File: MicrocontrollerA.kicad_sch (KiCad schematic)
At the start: 35 parts, among them J1 SWD Connector, J13 USB_B_Micro, SW1 SW_Push, SW2 SW_SPDT, SW3 SW_SPDT, U1 STM32F446RCTx, U5 TVS0500DRV, Y1 25 MHz

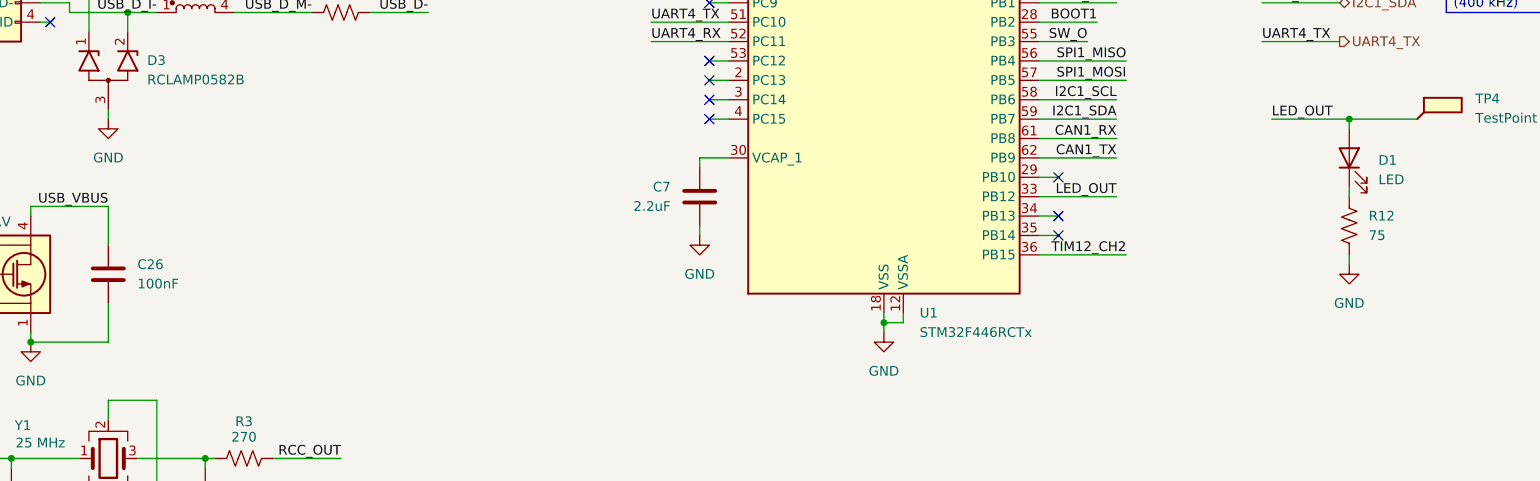
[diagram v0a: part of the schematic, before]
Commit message: Switch from variable to fixed 3.3V buck converter
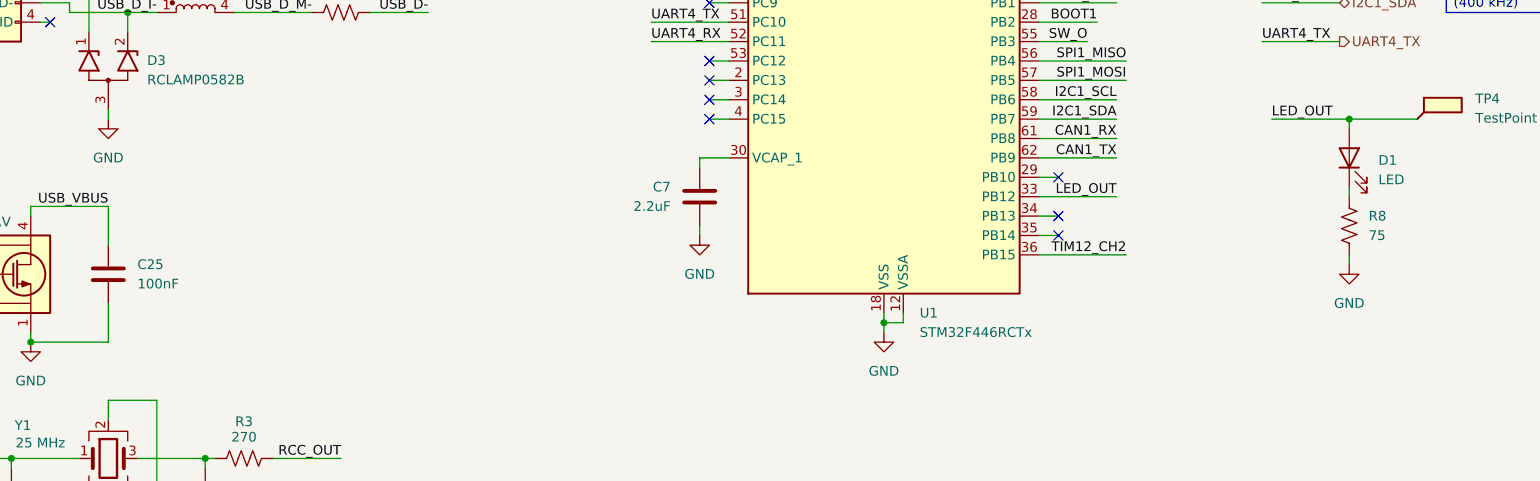
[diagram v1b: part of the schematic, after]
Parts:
- renumbered C26 to C25, R12 to R8
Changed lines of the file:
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@@
 		(dnp no)
 		(fields_autoplaced yes)
-		(property "Reference" "C26"
+		(property "Reference" "C25"
 			(at 50.8 146.0499 0)
 			(effects
@@
 			(project "XuLabPlatform"
 				(path "/71bb14ae-b730-4d22-a41d-cf68989dae2d/4b34bde8-cf26-4b12-b362-4972fe9ac1d6"
-					(reference "C26")
+					(reference "C25")
 					(unit 1)
 				)
@@
 		(dnp no)
 		(fields_autoplaced yes)
-		(property "Reference" "R12"
+		(property "Reference" "R8"
 			(at 212.09 139.6999 0)
 			(effects
@@
 			(project ""
 				(path "/71bb14ae-b730-4d22-a41d-cf68989dae2d/4b34bde8-cf26-4b12-b362-4972fe9ac1d6"
-					(reference "R12")
+					(reference "R8")
 					(unit 1)
 				)

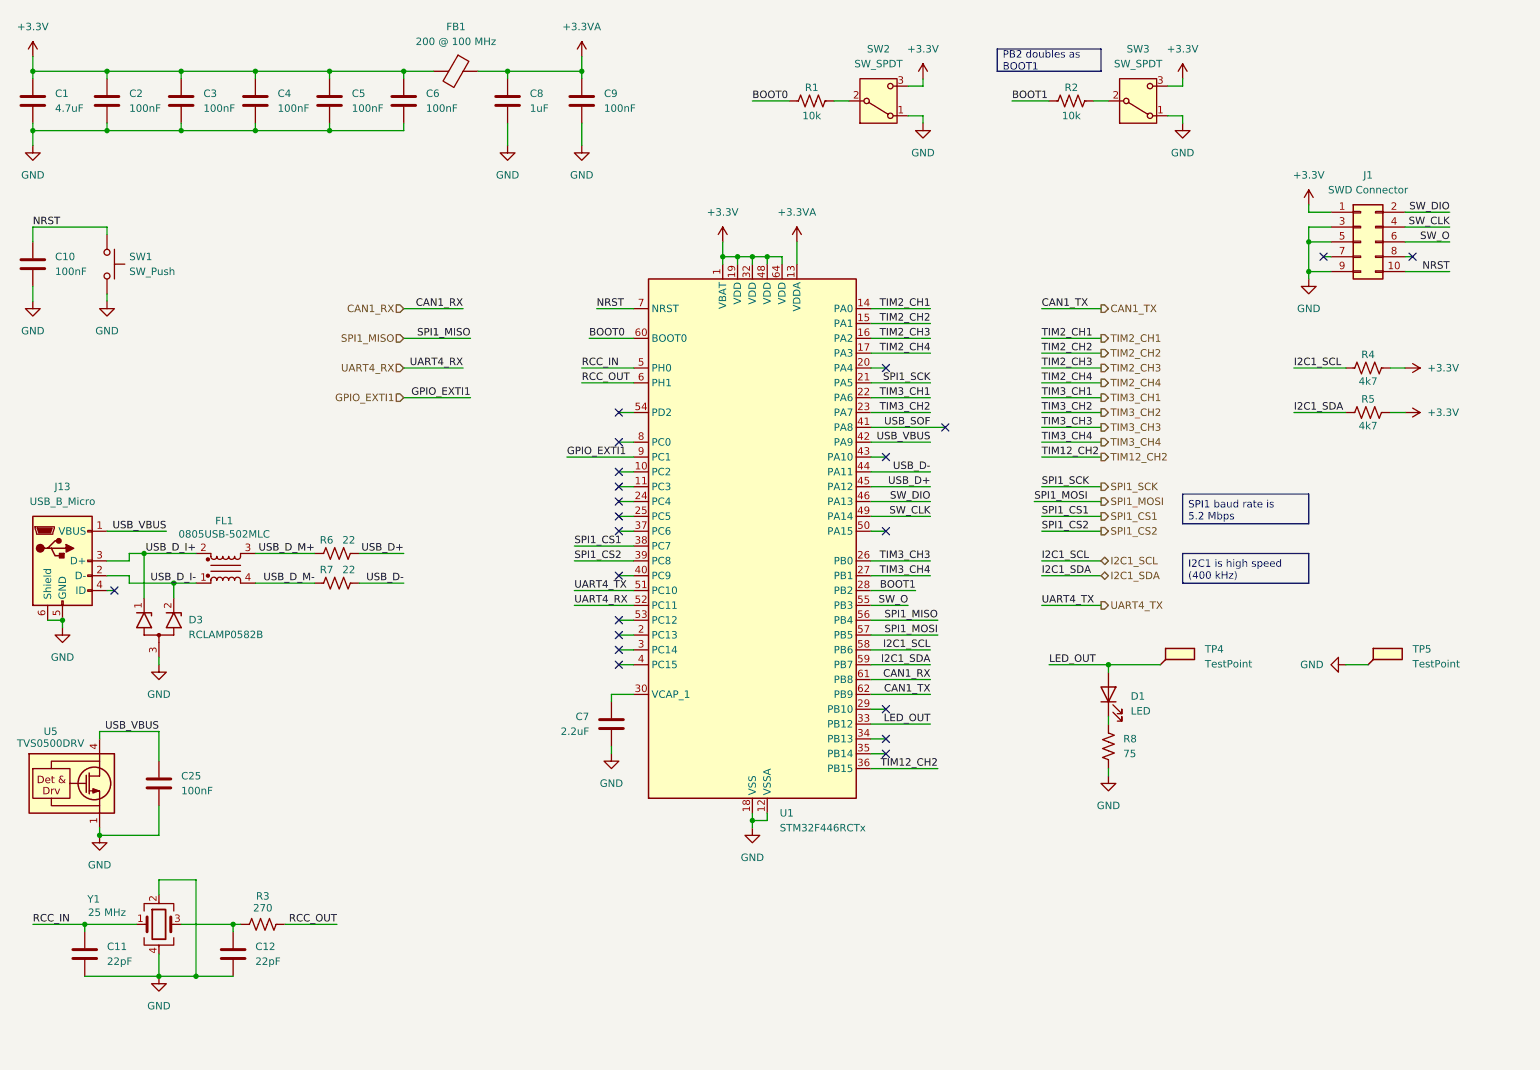
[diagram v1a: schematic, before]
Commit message: Change ferrite bead with TLV1117LV33 LDO for 3.3VA filtering
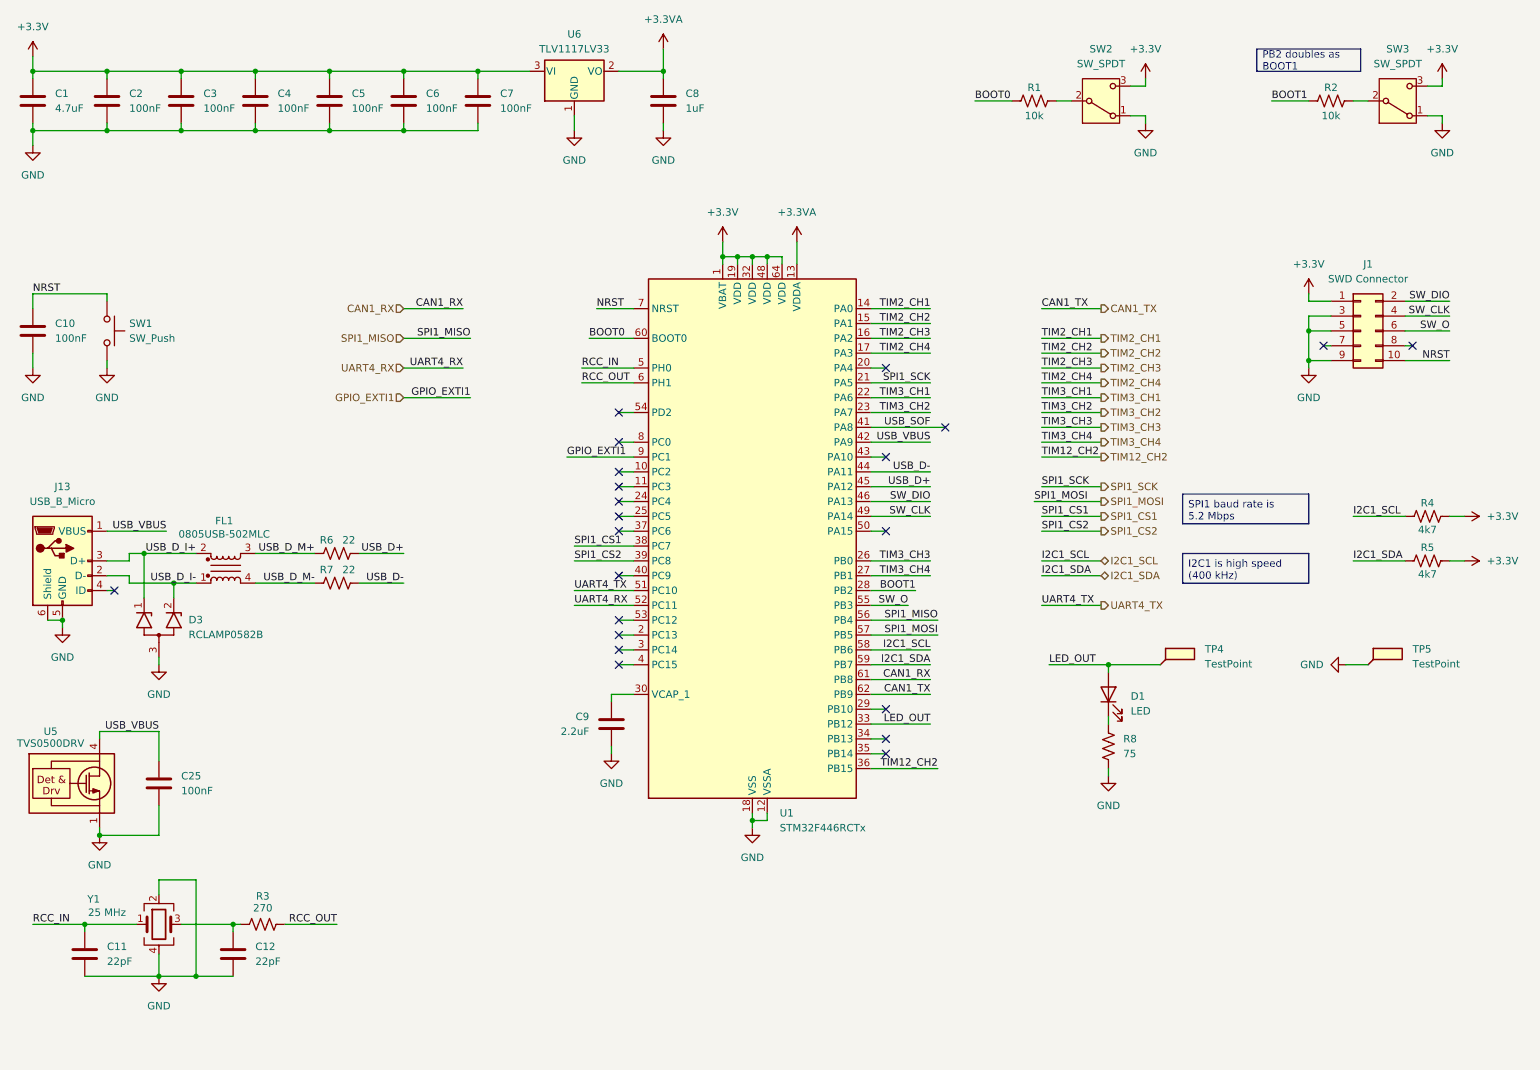
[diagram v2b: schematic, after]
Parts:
- removed FB1: 200 @ 100 MHz, Inductor_SMD:L_0805_2012Metric, symbol Device:FerriteBead
- added U6: TLV1117LV33, Package_TO_SOT_SMD:SOT-223-3_TabPin2, symbol Regulator_Linear:TLV1117-33
- renumbered C9 to C7, C7 to C9
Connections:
- net +3.3V: now also C7.1, U6.3 (VI)
- net +3.3VA: now also U6.2 (VO); no longer C7.1
- net GND: now also U6.1 (GND)
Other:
- moved on the sheet: C10, C7, J1, R1, R2, R4, R5, SW1, SW2, SW3

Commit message: Add rest of connections
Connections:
- net USB_D_I+: now also D3.2 (K2); no longer D3.1 (K1)
- net USB_D_I-: now also D3.1 (K1); no longer D3.2 (K2)
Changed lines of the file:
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@@
-	)
-	(junction
-		(at 49.53 113.03)
-		(diameter 0)
-		(color 0 0 0 0)
 	)
 	(junction
@@
 	)
 	(junction
+		(at 49.53 107.95)
+		(diameter 0)
+		(color 0 0 0 0)
+	)
+	(junction
 		(at 50.8 35.56)
 		(diameter 0)
@@
 	)
 	(junction
+		(at 44.45 113.03)
+		(diameter 0)
+		(color 0 0 0 0)
+	)
+	(junction
 		(at 88.9 35.56)
 		(diameter 0)
@@
 	)
 	(junction
-		(at 44.45 107.95)
-		(diameter 0)
-		(color 0 0 0 0)
-	)
-	(junction
 		(at 50.8 25.4)
 		(diameter 0)
@@
 	(wire
 		(pts
-			(xy 44.45 107.95) (xy 53.34 107.95)
+			(xy 41.91 107.95) (xy 49.53 107.95)
 		)
 		(stroke
@@
 	(wire
 		(pts
+			(xy 44.45 113.03) (xy 44.45 115.57)
+		)
+		(stroke
+			(width 0)
+			(type default)
+		)
+	)
+	(wire
+		(pts
 			(xy 153.67 57.15) (xy 153.67 58.42)
 		)
@@
 	(wire
 		(pts
-			(xy 49.53 113.03) (xy 49.53 115.57)
-		)
-		(stroke
-			(width 0)
-			(type default)
-		)
-	)
-	(wire
-		(pts
 			(xy 143.51 54.61) (xy 143.51 57.15)
 		)
@@
 	(wire
 		(pts
+			(xy 44.45 113.03) (xy 53.34 113.03)
+		)
+		(stroke
+			(width 0)
+			(type default)
+		)
+	)
+	(wire
+		(pts
 			(xy 156.21 54.61) (xy 156.21 58.42)
 		)
@@
 	(wire
 		(pts
-			(xy 49.53 113.03) (xy 53.34 113.03)
+			(xy 41.91 113.03) (xy 44.45 113.03)
 		)
 		(stroke
@@
 	(wire
 		(pts
+			(xy 49.53 107.95) (xy 53.34 107.95)
+		)
+		(stroke
+			(width 0)
+			(type default)
+		)
+	)
+	(wire
+		(pts
 			(xy 168.91 88.9) (xy 179.07 88.9)
 		)
@@
 	(wire
 		(pts
-			(xy 44.45 107.95) (xy 44.45 115.57)
-		)
-		(stroke
-			(width 0)
-			(type default)
-		)
-	)
-	(wire
-		(pts
 			(xy 198.12 96.52) (xy 208.28 96.52)
 		)
@@
 	(wire
 		(pts
-			(xy 41.91 107.95) (xy 44.45 107.95)
-		)
-		(stroke
-			(width 0)
-			(type default)
-		)
-	)
-	(wire
-		(pts
 			(xy 168.91 81.28) (xy 179.07 81.28)
 		)
@@
 	(wire
 		(pts
+			(xy 49.53 107.95) (xy 49.53 115.57)
+		)
+		(stroke
+			(width 0)
+			(type default)
+		)
+	)
+	(wire
+		(pts
 			(xy 215.9 27.94) (xy 215.9 26.67)
 		)
@@
 		)
 		(stroke
-			(width 0)
-			(type default)
-		)
-	)
-	(wire
-		(pts
-			(xy 41.91 113.03) (xy 49.53 113.03)
-		)
-		(stroke

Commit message: Replace zener diode footprints with generics
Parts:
- renumbered D3 to D2
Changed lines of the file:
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@@
 	(title_block
 		(title "MCU A - STM32F446RCT6")
-		(date "2025-11-12")
+		(date "2025-11-26")
 		(rev "A")
 		(company "CU Boulder Senior Design Team 29 - Xu Lab")
@@
 		(dnp no)
 		(fields_autoplaced yes)
-		(property "Reference" "D3"
+		(property "Reference" "D2"
 			(at 52.07 119.3164 90)
 			(effects
@@
 			(project ""
 				(path "/71bb14ae-b730-4d22-a41d-cf68989dae2d/4b34bde8-cf26-4b12-b362-4972fe9ac1d6"
-					(reference "D3")
+					(reference "D2")
 					(unit 1)
 				)

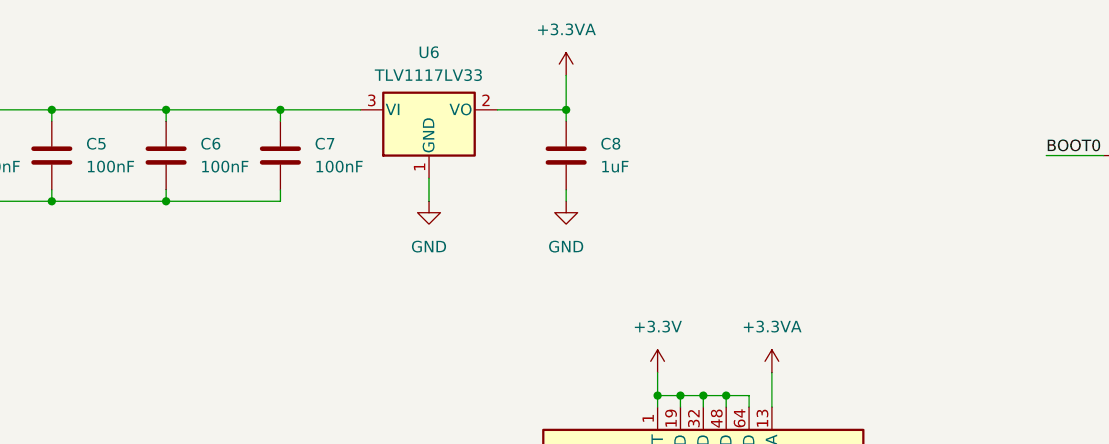
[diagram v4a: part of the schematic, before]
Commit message: Add ferrite bead and decoupling capacitors to analog power input
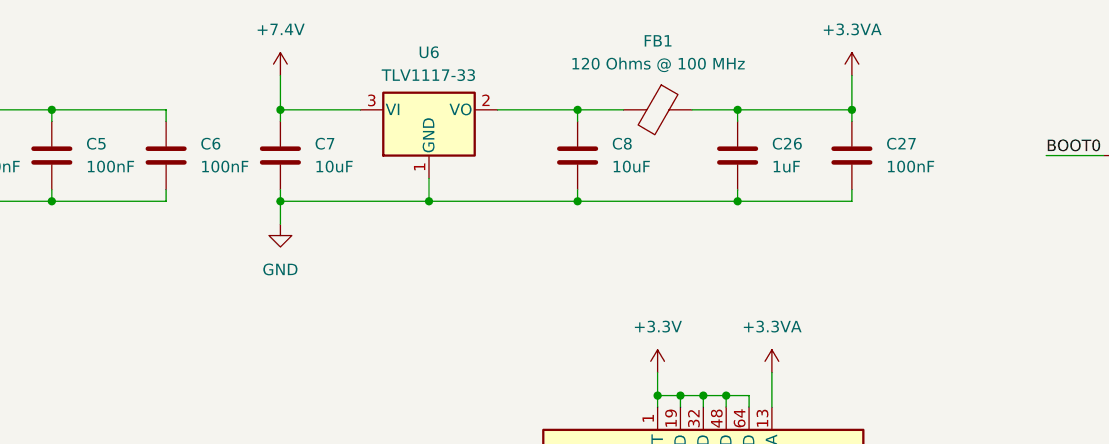
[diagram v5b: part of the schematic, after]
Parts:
- added C26: 1uF, Capacitor_SMD:C_0603_1608Metric, symbol Device:C
- added C27: 100nF, Capacitor_SMD:C_0402_1005Metric, symbol Device:C
- added FB1: 120 Ohms @ 100 MHz, Inductor_SMD:L_0805_2012Metric, symbol Device:FerriteBead
- C7: value 100nF -> 10uF; footprint Capacitor_SMD:C_0402_1005Metric -> Capacitor_SMD:C_1206_3216Metric; Listing https://www.digikey.com/en/products/detail/samsung-electro-mechanics/CL05A104KA5NNNC/3886701 -> https://www.digikey.com/en/products/detail/samsung-electro-mechanics/CL31B106KAHNNNE/3887462
- C8: value 1uF -> 10uF; footprint Capacitor_SMD:C_0603_1608Metric -> Capacitor_SMD:C_1206_3216Metric; Listing https://www.digikey.com/en/products/detail/samsung-electro-mechanics/CL10B105KO8NNNC/3886677 -> https://www.digikey.com/en/products/detail/samsung-electro-mechanics/CL31B106KAHNNNE/3887462
- U6: value TLV1117LV33 -> TLV1117-33; Listing https://www.digikey.com/en/products/detail/texas-instruments/TLV1117LV33DCYR/2666508 -> https://www.digikey.com/en/products/detail/texas-instruments/TLV1117-33IDCYR/1216719
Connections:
- net +3.3V: no longer C7.1, U6.3 (VI)
- net +3.3VA: now also C26.1, C27.1, FB1.1; no longer C8.1, U6.2 (VO)
- net GND: now also C26.2, C27.2
- new net: C8.1, FB1.2, U6.2 (VO)
- new net +7.4V: C7.1, U6.3 (VI)

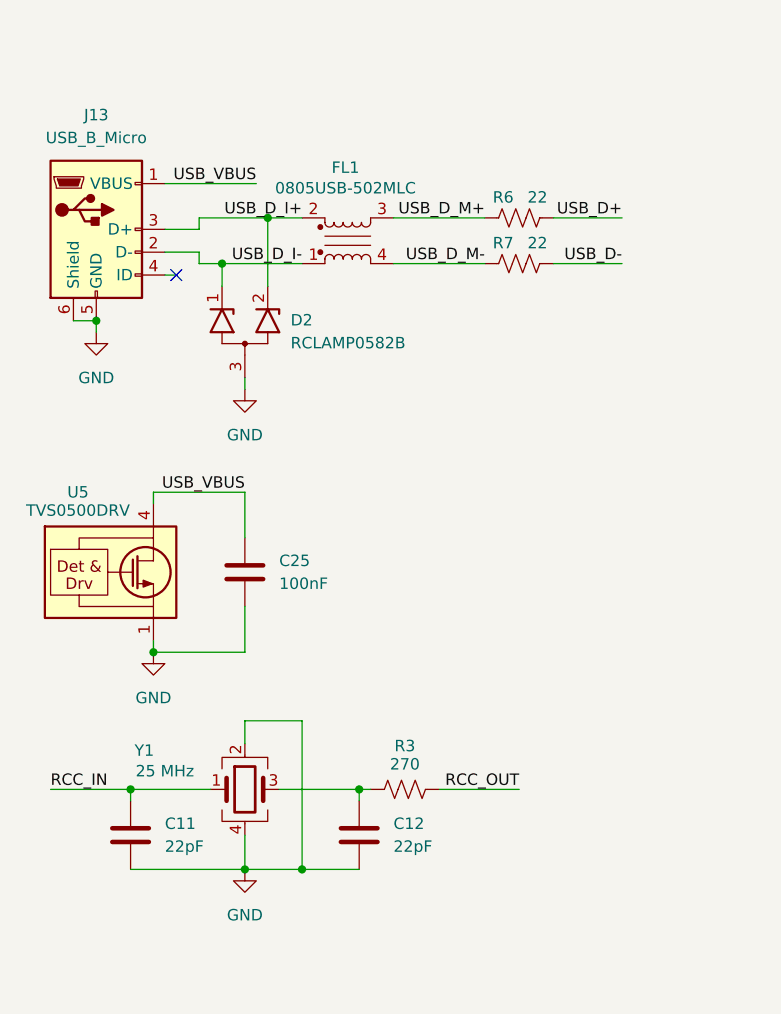
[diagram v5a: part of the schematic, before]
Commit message: Add 3.3 V voltage divider to 5 V VBUS line
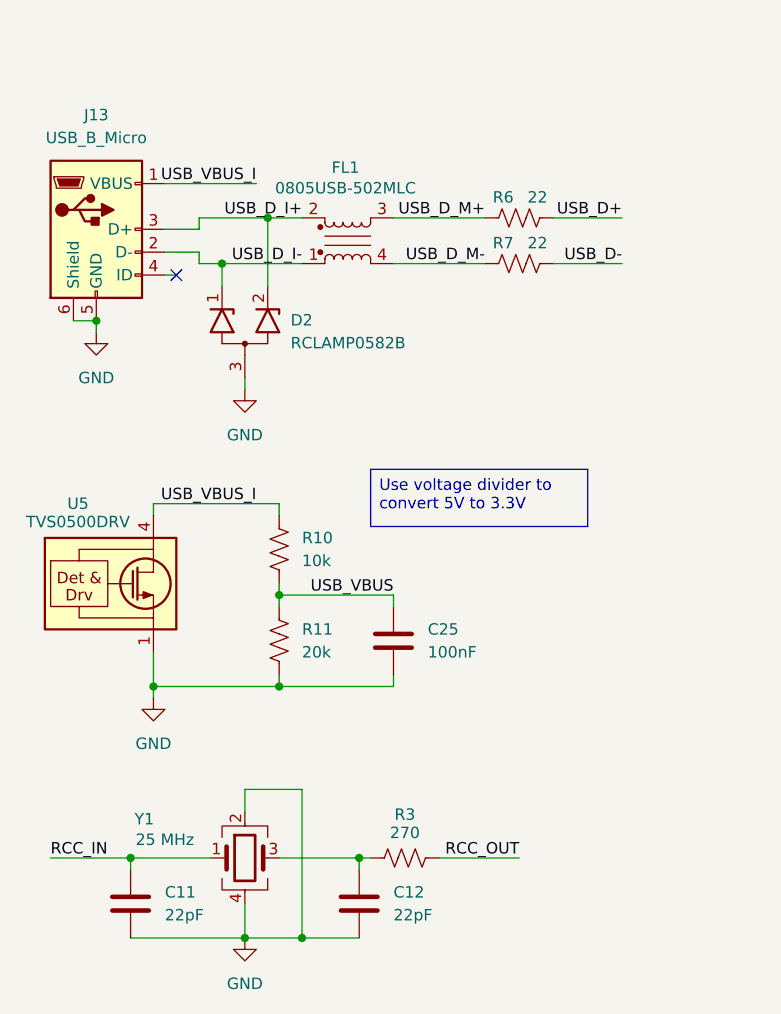
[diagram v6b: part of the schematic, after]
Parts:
- added R10: 10k, Resistor_SMD:R_0603_1608Metric, symbol Device:R_US
- added R11: 20k, Resistor_SMD:R_0603_1608Metric, symbol Device:R_US
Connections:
- net GND: now also R11.2
- net USB_VBUS: now also R10.2, R11.1; no longer J13.1 (VBUS), U5.4 (IN), U5.5 (IN), U5.6 (IN)
- new net USB_VBUS_I: J13.1 (VBUS), R10.1, U5.4 (IN), U5.5 (IN), U5.6 (IN)
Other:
- moved on the sheet: C11, C12, C25, R3, U5, Y1
